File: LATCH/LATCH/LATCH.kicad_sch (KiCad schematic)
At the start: 39 parts, among them J1 39281123, J4 39281083, J5 39281063, K1 G6B-2214P-US DC12, K2 G6B-2214P-US DC12, K4 G6B-2214P-US DC12, Q1 PMOS IRF9540, Q2 PMOS IRF9540, Q3 PMOS IRF9540, SW1 SW_Push, SW2 SW_Push, SW3 SW_Push

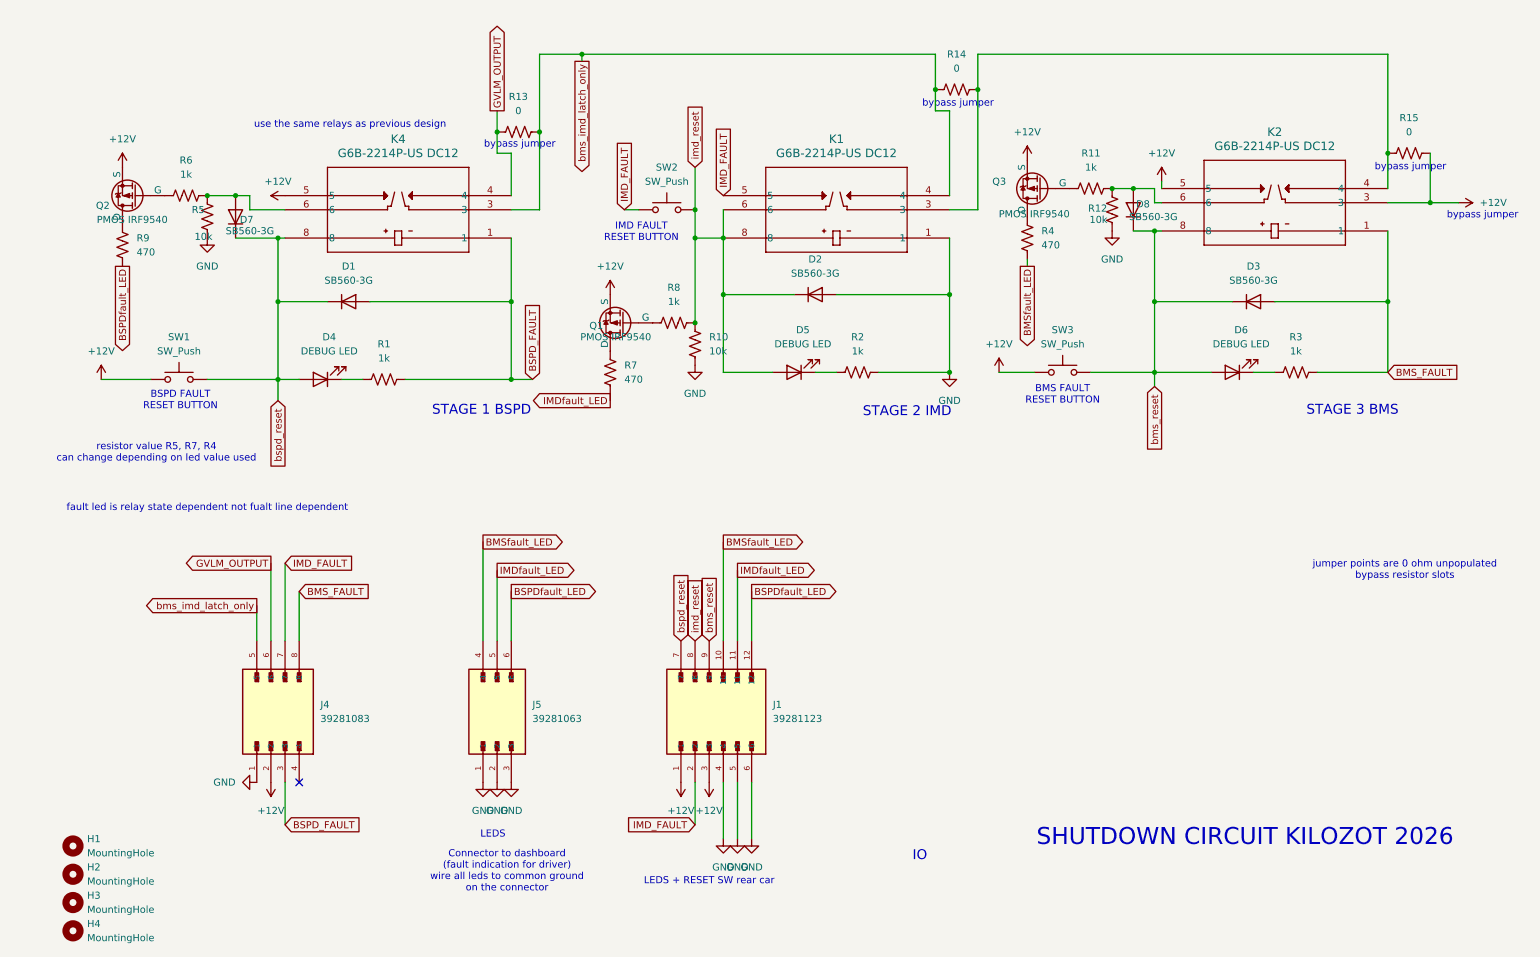
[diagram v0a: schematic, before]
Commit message: Changed a buncha stuff on other ppl's board. established new branch
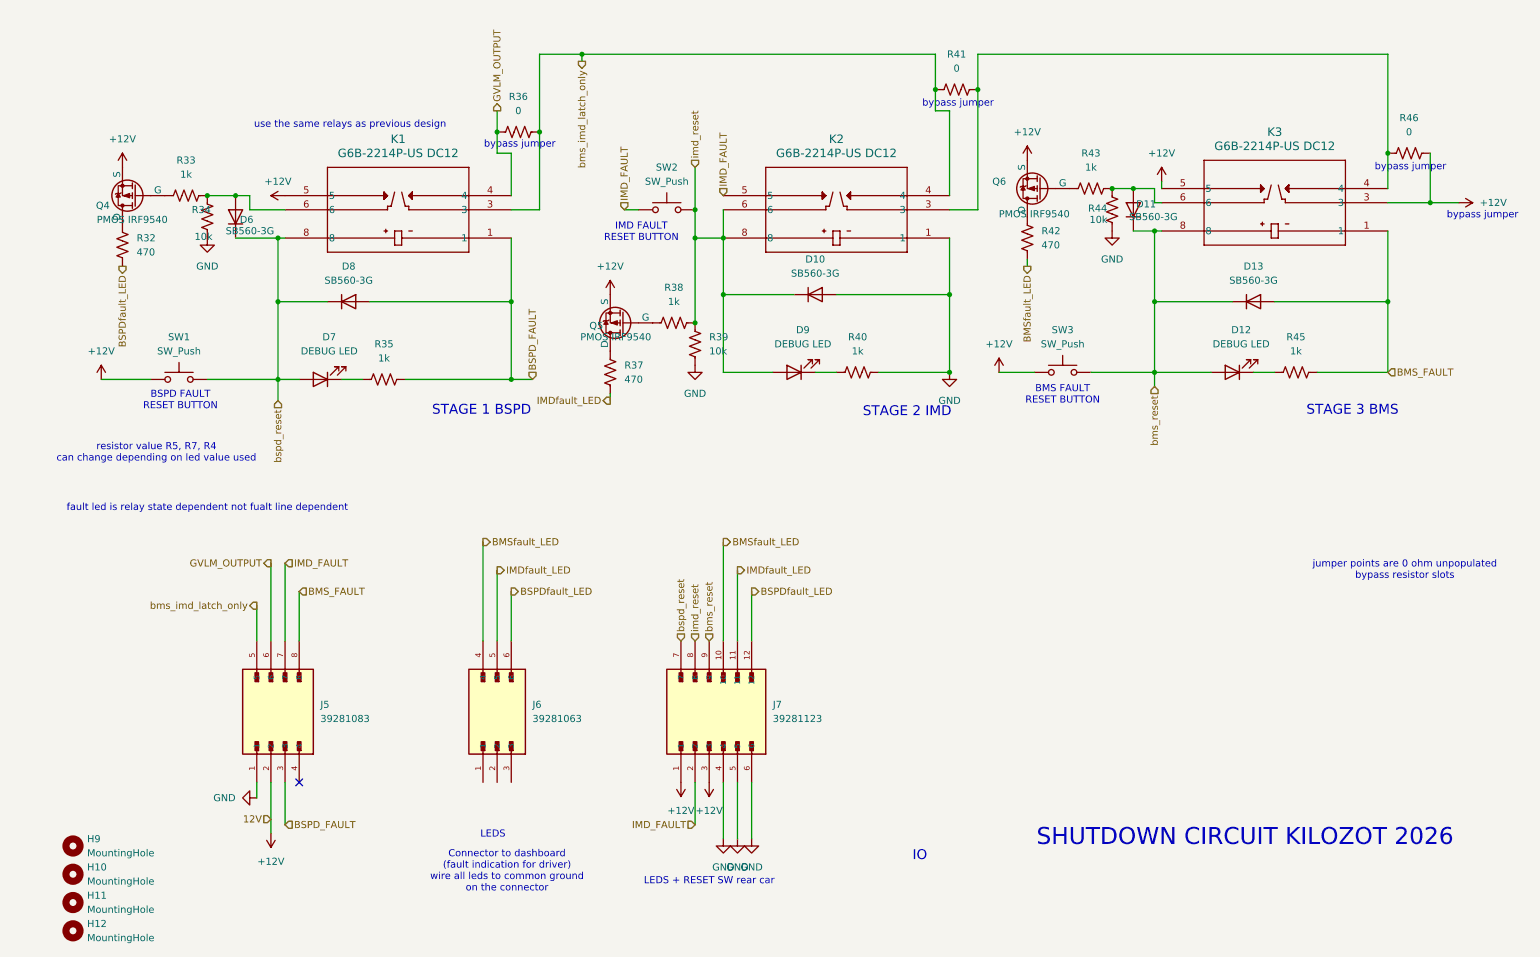
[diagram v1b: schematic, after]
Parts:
- renumbered D2 to D10, D8 to D11, D6 to D12, D3 to D13, D7 to D6, D4 to D7, D1 to D8, D5 to D9, H2 to H10, H3 to H11, H4 to H12, H1 to H9, J4 to J5, J5 to J6, J1 to J7, K4 to K1, K1 to K2, K2 to K3, Q2 to Q4, Q1 to Q5, Q3 to Q6, R9 to R32, R6 to R33, R5 to R34, R1 to R35, R13 to R36, R7 to R37, R8 to R38, R10 to R39, R2 to R40, R14 to R41, R4 to R42, R11 to R43, R12 to R44, R3 to R45, R15 to R46
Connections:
- net GND: no longer J6.1, J6.2, J6.3

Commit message: day 2 grind
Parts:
- removed J5: 39281083, 1MyCustomLibrary:MOLEX_39281083, symbol 39281083:39281083
- renumbered J6 to J10, J7 to J11, R32 to R33, R33 to R34, R34 to R35, R35 to R36, R36 to R37, R37 to R38, R38 to R39, R39 to R40, R40 to R41, R41 to R42, R42 to R43, R43 to R44, R44 to R45, R45 to R46, R46 to R47
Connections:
- net GND: now also J10.1, J10.2, J10.3
- no-connect marks 1 -> 0

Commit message: hopefully this lets avadi pull
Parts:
- removed K2: G6B-2214P-US DC12, 1MyCustomLibrary:RELAY_G6B-2114P-US_OMR, symbol relay g6b:G6B-2214P-US_DC12
- added K1: G6B-2214P-US DC12, footprints:DPSTrelay, symbol relay g6b:G6B-2214P-US_DC12
- J10: footprint 1MyCustomLibrary:MOLEX_39281063 -> footprints:Molex_Mini-Fit_Jr_5566-06A_2x03_P4.20mm_Vertical
- J11: footprint 1MyCustomLibrary:MOLEX_39281123 -> footprints:12pSTminifit
- K2: renamed from K1; footprint 1MyCustomLibrary:RELAY_G6B-2114P-US_OMR -> footprints:DPSTrelay
- K3: footprint 1MyCustomLibrary:RELAY_G6B-2114P-US_OMR -> footprints:DPSTrelay
- renumbered Q4 to Q5, Q5 to Q6, Q6 to Q7, R33 to R34, R34 to R35, R35 to R36, R36 to R37, R37 to R38, R38 to R39, R39 to R40, R40 to R41, R41 to R42, R42 to R43, R43 to R44, R44 to R45, R45 to R46, R46 to R47, R47 to R48
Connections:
- net +12V: now also K1.5; no longer K2.5
- net BSPD_FAULT: now also K1.1; no longer K2.1
- net GND: now also K2.1
- net GVLM_OUTPUT: now also K1.4; no longer K2.4
- net IMD_FAULT: now also K2.5
- net bms_imd_latch_only: now also K2.4, K1.3; no longer K2.3
- net bspd_reset: now also K1.8; no longer K2.8
- net imd_reset: now also K2.6, K2.8
- net at K3.4, R43.2, R48.1: now also K2.3
- net at D6.2 (A), R35.2, R36.1: now also K1.6; no longer K2.6
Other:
- moved on the sheet: K2

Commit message: rough layout done
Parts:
- removed D10, D11, D13, D6, D8: SB560-3G, Diode_THT:D_DO-201_P15.24mm_Horizontal, symbol Diode:1N4148WT
- removed H10, H11, H12, H9: MountingHole, MountingHole:MountingHole_3.2mm_M3, symbol Mechanical:MountingHole
- removed R34, R39, R44: 470, Resistor_THT:R_Axial_DIN0207_L6.3mm_D2.5mm_P10.16mm_Horizontal, symbol Device:R_US
- removed R38, R43, R48: 0, Resistor_THT:R_Axial_DIN0207_L6.3mm_D2.5mm_P10.16mm_Horizontal, symbol Device:R_US
- added D1, D10, D11, D6, D8: D, Diode_SMD:D_0603_1608Metric, symbol Device:D
- J10: value 39281063 -> Dash
- J11: value 39281123 -> BBC
- Q5, Q6, Q7: footprint Package_TO_SOT_THT:TO-220-3_Vertical -> Package_TO_SOT_THT:TO-220F-3_Horizontal_TabDown
- R35, R36, R37, R40, R41, R42, R45, R46, R47: footprint Resistor_THT:R_Axial_DIN0207_L6.3mm_D2.5mm_P10.16mm_Horizontal -> Resistor_SMD:R_0805_2012Metric_Pad1.20x1.40mm_HandSolder
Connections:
- net BMS_FAULT: now also D10.2 (A)
- net BMSfault_LED: now also Q7.2 (D)
- net BSPD_FAULT: now also D1.2 (A)
- net BSPDfault_LED: now also Q5.2 (D)
- net GND: now also D8.2 (A)
- net IMDfault_LED: now also Q6.2 (D)
- net bms_reset: now also D10.1 (K), D11.1 (K)
- net bspd_reset: now also D1.1 (K), D6.1 (K)
- net imd_reset: now also D8.1 (K)
- net at K3.6, R45.2, R46.1: now also D11.2 (A)
- net at K1.6, R35.2, R36.1: now also D6.2 (A)

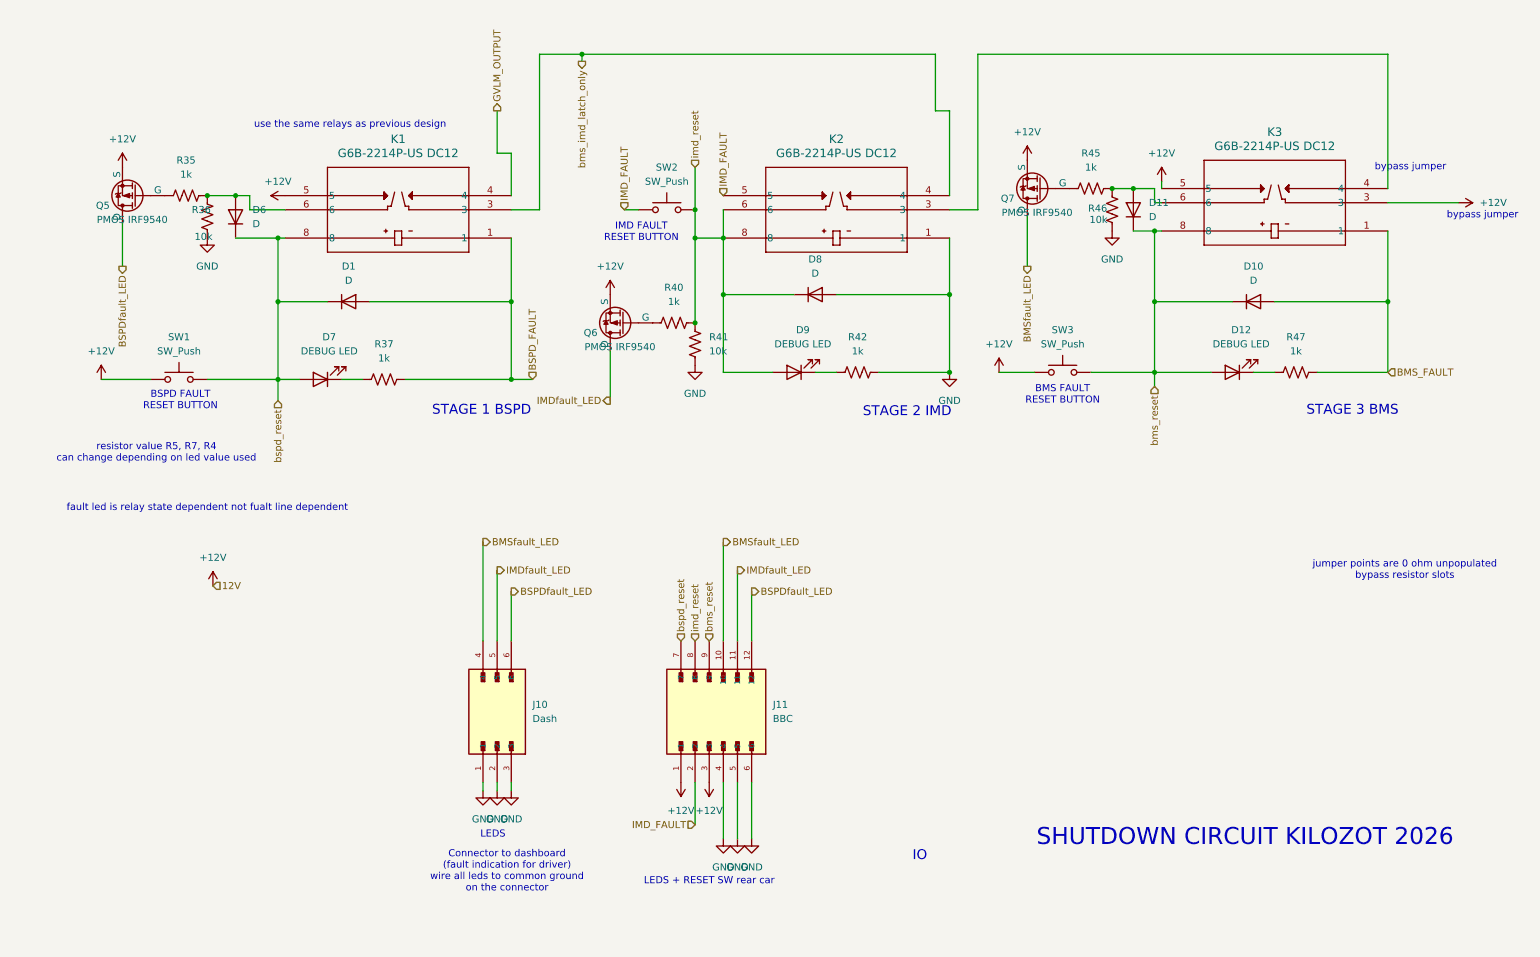
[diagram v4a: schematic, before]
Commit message: silkscreen and some fuses or something
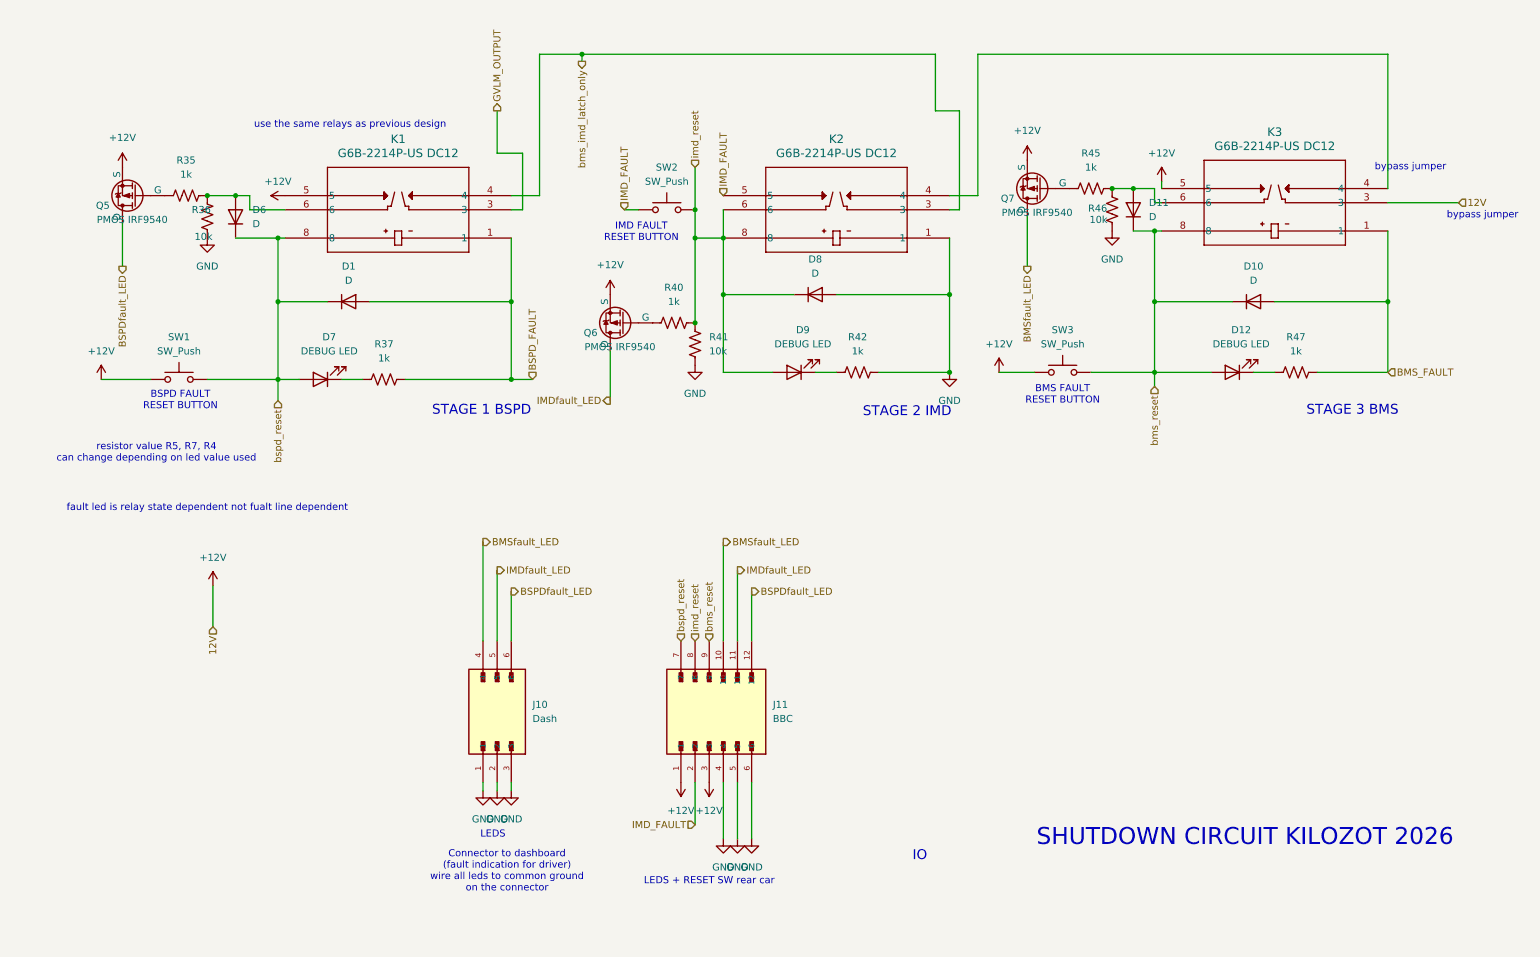
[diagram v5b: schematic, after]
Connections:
- net GVLM_OUTPUT: now also K1.3; no longer K1.4
- net bms_imd_latch_only: now also K1.4, K2.3; no longer K1.3, K2.4
- net at K3.4: now also K2.4; no longer K2.3
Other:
- note removed: "jumper points are 0 ohm unpopulated bypass resistor slots"

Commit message: I think think this is final but need to defuck the BOM
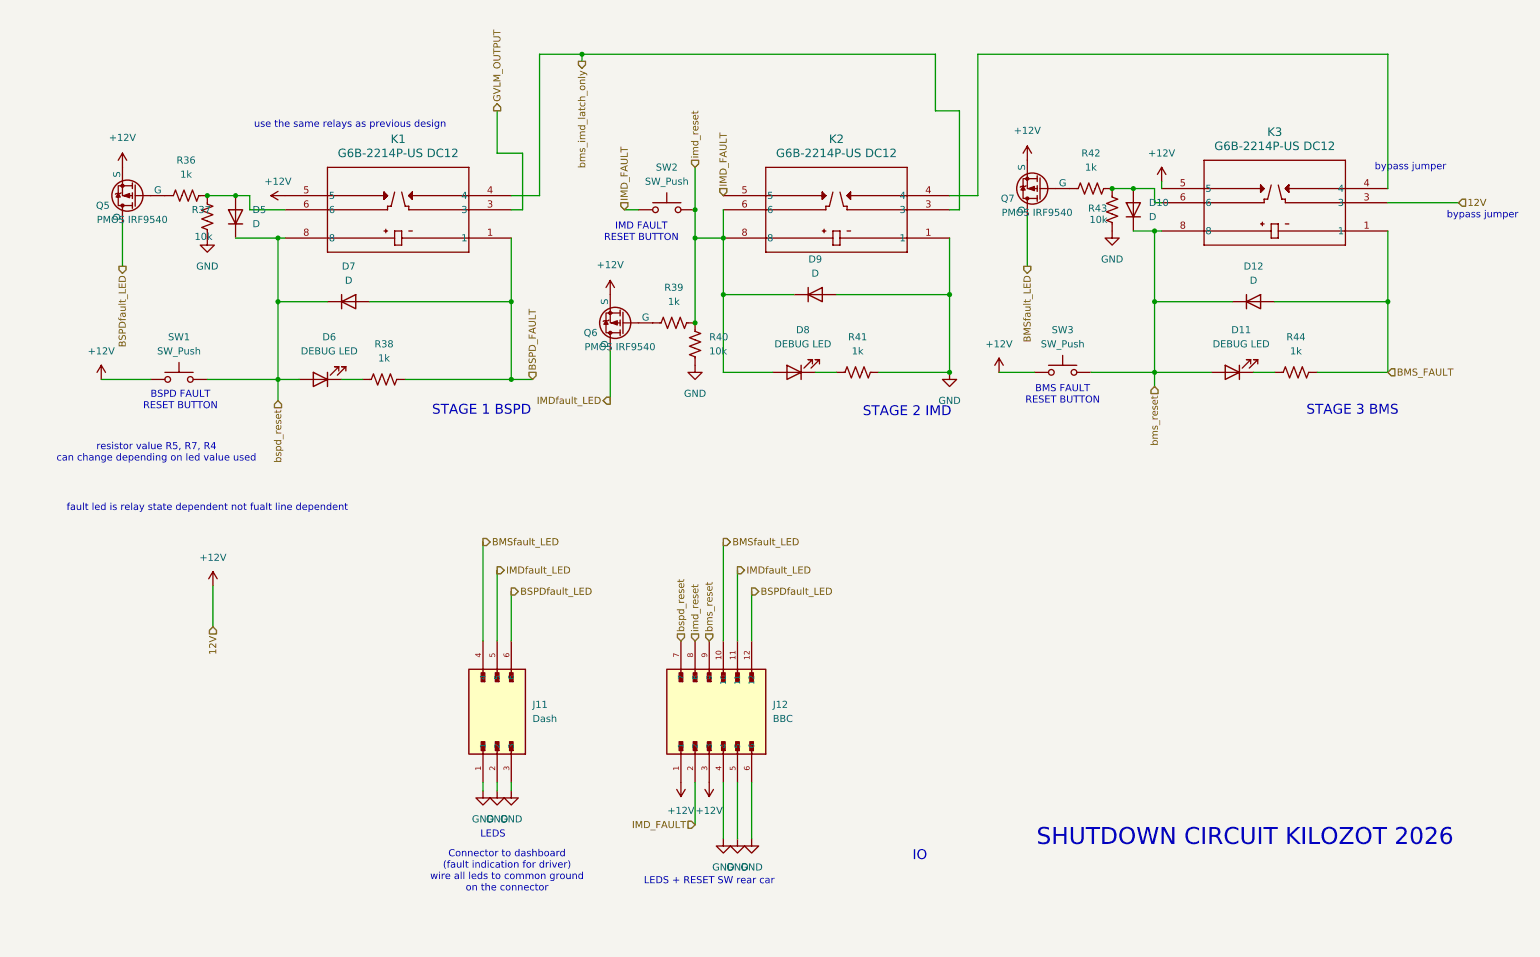
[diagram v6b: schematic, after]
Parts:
- removed D1: D, Diode_SMD:D_0603_1608Metric, symbol Device:D
- added D7: D, Diode_SMD:D_0603_1608Metric, symbol Device:D
- renumbered D11 to D10, D12 to D11, D10 to D12, D6 to D5, D7 to D6, D9 to D8, D8 to D9, J10 to J11, J11 to J12, R35 to R36, R36 to R37, R37 to R38, R40 to R39, R41 to R40, R42 to R41, R45 to R42, R46 to R43, R47 to R44
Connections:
- net BSPD_FAULT: now also D7.2 (A)
- net bspd_reset: now also D7.1 (K)
